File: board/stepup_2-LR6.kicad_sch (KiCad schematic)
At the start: 17 parts

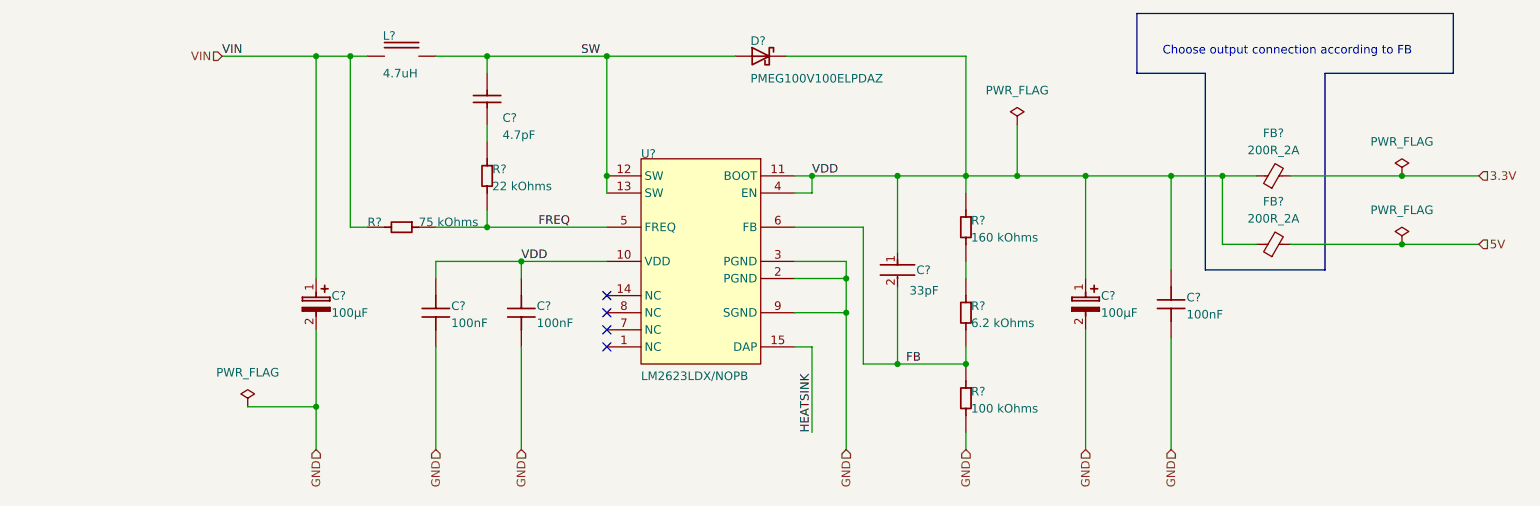
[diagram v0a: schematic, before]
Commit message: switched edge connectors to use the correct footprints and renamed local libraries to fit with the edgy naming convention
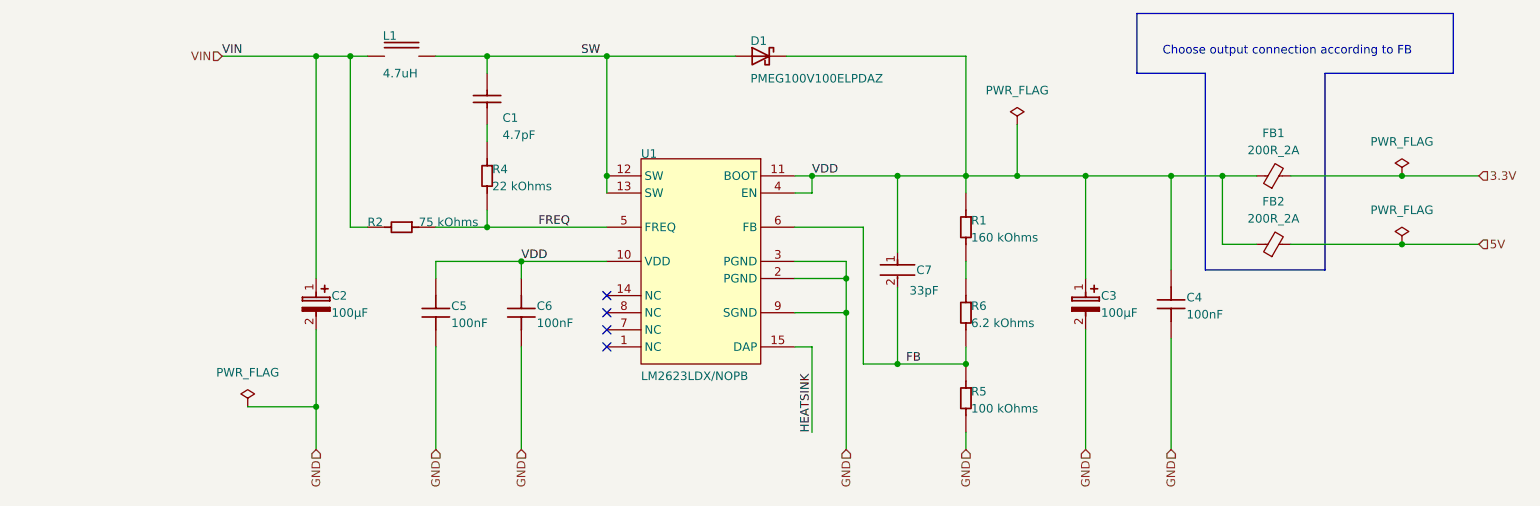
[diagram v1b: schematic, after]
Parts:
- C2, C3: renamed from C?; footprint stpup:CAPMP7344X43-T_V -> b132:CAPMP7344X43-T_V
- D1: renamed from D?; footprint stpup:PMEG100V100ELPDAZ -> b132:PMEG100V100ELPDAZ
- L1: renamed from L?; footprint stpup:WURTH 5040 -> b132:WURTH 5040
- U1: renamed from U?; footprint stpup:NHE0014A_V -> b132:NHE0014A_V
- gave numbers to parts that had none: 12
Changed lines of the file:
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@@
   (symbol (lib_id "step-up_2cell:1_Capacitor") (at 111.76 113.03 0) (unit 1)
     (in_bom yes) (on_board yes)
-    (property "Reference" "C?" (id 0) (at 114.046 112.776 0)
+    (property "Reference" "C5" (id 0) (at 114.046 112.776 0)
       (effects (font (size 1.27 1.27)) (justify left bottom))
     )
@@
   (symbol (lib_id "Device:FerriteBead_Small") (at 236.22 102.87 90) (unit 1)
     (in_bom yes) (on_board yes) (fields_autoplaced)
-    (property "Reference" "FB?" (id 0) (at 236.1819 96.52 90))
+    (property "Reference" "FB2" (id 0) (at 236.1819 96.52 90))
     (property "Value" "200R_2A" (id 1) (at 236.1819 99.06 90))
     (property "Footprint" "Inductor_SMD:L_0805_2012Metric" (id 2) (at 236.22 104.648 90)
@@
   (symbol (lib_id "step-up_2cell:3_T495X477K010ATE100") (at 208.28 107.95 0) (unit 1)
     (in_bom yes) (on_board yes)
-    (property "Reference" "C?" (id 0) (at 210.566 111.252 0)
+    (property "Reference" "C3" (id 0) (at 210.566 111.252 0)
       (effects (font (size 1.27 1.27)) (justify left bottom))
     )
@@
       (effects (font (size 1.27 1.27)) (justify left bottom) hide)
     )
-    (property "Footprint" "stpup:CAPMP7344X43-T_V" (id 2) (at 208.28 107.95 0)
+    (property "Footprint" "b132:CAPMP7344X43-T_V" (id 2) (at 208.28 107.95 0)
       (effects (font (size 1.27 1.27)) hide)
     )
@@
   (symbol (lib_id "power:PWR_FLAG") (at 255.27 92.71 0) (unit 1)
     (in_bom yes) (on_board yes) (fields_autoplaced)
-    (property "Reference" "#FLG?" (id 0) (at 255.27 90.805 0)
+    (property "Reference" "#FLG0103" (id 0) (at 255.27 90.805 0)
       (effects (font (size 1.27 1.27)) hide)
     )
@@
   (symbol (lib_id "step-up_2cell:0_Inductor") (at 106.68 74.93 0) (unit 1)
     (in_bom yes) (on_board yes)
-    (property "Reference" "L?" (id 0) (at 103.886 72.644 0)
+    (property "Reference" "L1" (id 0) (at 103.886 72.644 0)
       (effects (font (size 1.27 1.27)) (justify left bottom))
     )
@@
       (effects (font (size 1.27 1.27)) (justify left bottom))
     )
-    (property "Footprint" "stpup:WURTH 5040" (id 2) (at 106.68 74.93 0)
+    (property "Footprint" "b132:WURTH 5040" (id 2) (at 106.68 74.93 0)
       (effects (font (size 1.27 1.27)) hide)
     )
@@
   (symbol (lib_id "step-up_2cell:1_Resistor") (at 190.5 113.03 0) (unit 1)
     (in_bom yes) (on_board yes)
-    (property "Reference" "R?" (id 0) (at 191.262 112.776 0)
+    (property "Reference" "R6" (id 0) (at 191.262 112.776 0)
       (effects (font (size 1.27 1.27)) (justify left bottom))
     )
@@
   (symbol (lib_id "power:PWR_FLAG") (at 198.12 85.09 0) (unit 1)
     (in_bom yes) (on_board yes) (fields_autoplaced)
-    (property "Reference" "#FLG?" (id 0) (at 198.12 83.185 0)
+    (property "Reference" "#FLG0101" (id 0) (at 198.12 83.185 0)
       (effects (font (size 1.27 1.27)) hide)
     )
@@
   (symbol (lib_id "step-up_2cell:1_Capacitor") (at 220.98 111.76 0) (unit 1)
     (in_bom yes) (on_board yes)
-    (property "Reference" "C?" (id 0) (at 223.266 111.506 0)
+    (property "Reference" "C4" (id 0) (at 223.266 111.506 0)
       (effects (font (size 1.27 1.27)) (justify left bottom))
     )
@@
   (symbol (lib_id "Device:FerriteBead_Small") (at 236.22 92.71 90) (unit 1)
     (in_bom yes) (on_board yes) (fields_autoplaced)
-    (property "Reference" "FB?" (id 0) (at 236.1819 86.36 90))
+    (property "Reference" "FB1" (id 0) (at 236.1819 86.36 90))
     (property "Value" "200R_2A" (id 1) (at 236.1819 88.9 90))
     (property "Footprint" "Inductor_SMD:L_0805_2012Metric" (id 2) (at 236.22 94.488 90)
@@
   (symbol (lib_id "step-up_2cell:0_PM-DCDC-LM2623LD-15") (at 142.24 90.17 0) (unit 1)
     (in_bom yes) (on_board yes)
-    (property "Reference" "U?" (id 0) (at 142.24 90.17 0)
+    (property "Reference" "U1" (id 0) (at 142.24 90.17 0)
       (effects (font (size 1.27 1.27)) (justify left bottom))
     )
@@
       (effects (font (size 1.27 1.27)) (justify left bottom))
     )
-    (property "Footprint" "stpup:NHE0014A_V" (id 2) (at 142.24 90.17 0)
+    (property "Footprint" "b132:NHE0014A_V" (id 2) (at 142.24 90.17 0)
       (effects (font (size 1.27 1.27)) hide)
     )
@@
   (symbol (lib_id "step-up_2cell:3_T495X477K010ATE100") (at 93.98 107.95 0) (unit 1)
     (in_bom yes) (on_board yes)
-    (property "Reference" "C?" (id 0) (at 96.266 111.252 0)
+    (property "Reference" "C2" (id 0) (at 96.266 111.252 0)
       (effects (font (size 1.27 1.27)) (justify left bottom))
     )
@@
       (effects (font (size 1.27 1.27)) (justify left bottom) hide)
     )
-    (property "Footprint" "stpup:CAPMP7344X43-T_V" (id 2) (at 93.98 107.95 0)
+    (property "Footprint" "b132:CAPMP7344X43-T_V" (id 2) (at 93.98 107.95 0)
       (effects (font (size 1.27 1.27)) hide)
     )
@@
   (symbol (lib_id "step-up_2cell:1_Resistor") (at 190.5 125.73 0) (unit 1)
     (in_bom yes) (on_board yes)
-    (property "Reference" "R?" (id 0) (at 191.262 125.476 0)
+    (property "Reference" "R5" (id 0) (at 191.262 125.476 0)
       (effects (font (size 1.27 1.27)) (justify left bottom))
     )
@@
   (symbol (lib_id "step-up_2cell:0_b4654b650e69147ec39a6b967a45e02") (at 180.34 104.14 0) (unit 1)
     (in_bom yes) (on_board yes)
-    (property "Reference" "C?" (id 0) (at 183.134 107.442 0)
+    (property "Reference" "C7" (id 0) (at 183.134 107.442 0)
       (effects (font (size 1.27 1.27)) (justify left bottom))
     )
@@
   (symbol (lib_id "step-up_2cell:1_CAP-NP-2") (at 119.38 85.09 0) (unit 1)
     (in_bom yes) (on_board yes)
-    (property "Reference" "C?" (id 0) (at 121.666 84.836 0)
+    (property "Reference" "C1" (id 0) (at 121.666 84.836 0)
       (effects (font (size 1.27 1.27)) (justify left bottom))
     )
@@
   (symbol (lib_id "step-up_2cell:1_Capacitor") (at 124.46 113.03 0) (unit 1)
     (in_bom yes) (on_board yes)
-    (property "Reference" "C?" (id 0) (at 126.746 112.776 0)
+    (property "Reference" "C6" (id 0) (at 126.746 112.776 0)
       (effects (font (size 1.27 1.27)) (justify left bottom))
     )
@@
   (symbol (lib_id "step-up_2cell:0_Resistor") (at 106.68 100.33 0) (unit 1)
     (in_bom yes) (on_board yes)
-    (property "Reference" "R?" (id 0) (at 101.6 100.33 0)
+    (property "Reference" "R2" (id 0) (at 101.6 100.33 0)
       (effects (font (size 1.27 1.27)) (justify left bottom))
     )
@@
   (symbol (lib_id "power:PWR_FLAG") (at 83.82 127 0) (unit 1)
     (in_bom yes) (on_board yes) (fields_autoplaced)
-    (property "Reference" "#FLG?" (id 0) (at 83.82 125.095 0)
+    (property "Reference" "#FLG0102" (id 0) (at 83.82 125.095 0)
       (effects (font (size 1.27 1.27)) hide)
     )
@@
   (symbol (lib_id "power:PWR_FLAG") (at 255.27 102.87 0) (unit 1)
     (in_bom yes) (on_board yes) (fields_autoplaced)
-    (property "Reference" "#FLG?" (id 0) (at 255.27 100.965 0)
+    (property "Reference" "#FLG0104" (id 0) (at 255.27 100.965 0)
       (effects (font (size 1.27 1.27)) hide)
     )
@@
   (symbol (lib_id "step-up_2cell:1_Resistor") (at 190.5 100.33 0) (unit 1)
     (in_bom yes) (on_board yes)
-    (property "Reference" "R?" (id 0) (at 191.262 100.076 0)
+    (property "Reference" "R1" (id 0) (at 191.262 100.076 0)
       (effects (font (size 1.27 1.27)) (justify left bottom))
     )
@@
   (symbol (lib_id "step-up_2cell:1_Resistor") (at 119.38 92.71 0) (unit 1)
     (in_bom yes) (on_board yes)
-    (property "Reference" "R?" (id 0) (at 120.142 92.456 0)
+    (property "Reference" "R4" (id 0) (at 120.142 92.456 0)
       (effects (font (size 1.27 1.27)) (justify left bottom))
     )
@@
   (symbol (lib_id "step-up_2cell:0_mirrored_PMEG100V100ELPD") (at 161.29 74.93 0) (unit 1)
     (in_bom yes) (on_board yes)
-    (property "Reference" "D?" (id 0) (at 158.496 73.406 0)
+    (property "Reference" "D1" (id 0) (at 158.496 73.406 0)
       (effects (font (size 1.27 1.27)) (justify left bottom))
     )
@@
       (effects (font (size 1.27 1.27)) (justify left bottom))
     )
-    (property "Footprint" "stpup:PMEG100V100ELPDAZ" (id 2) (at 161.29 74.93 0)
-      (effects (font (size 1.27 1.27)) hide)
-    )
+    (property "Footprint" "b132:PMEG100V100ELPDAZ" (id 2) (at 161.29 74.93 0)
+      (effects (font (size 1.27 1.27)) hide)
+    )

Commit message: changed constraints to work as a 2 layer board, changed symbols to kicad native
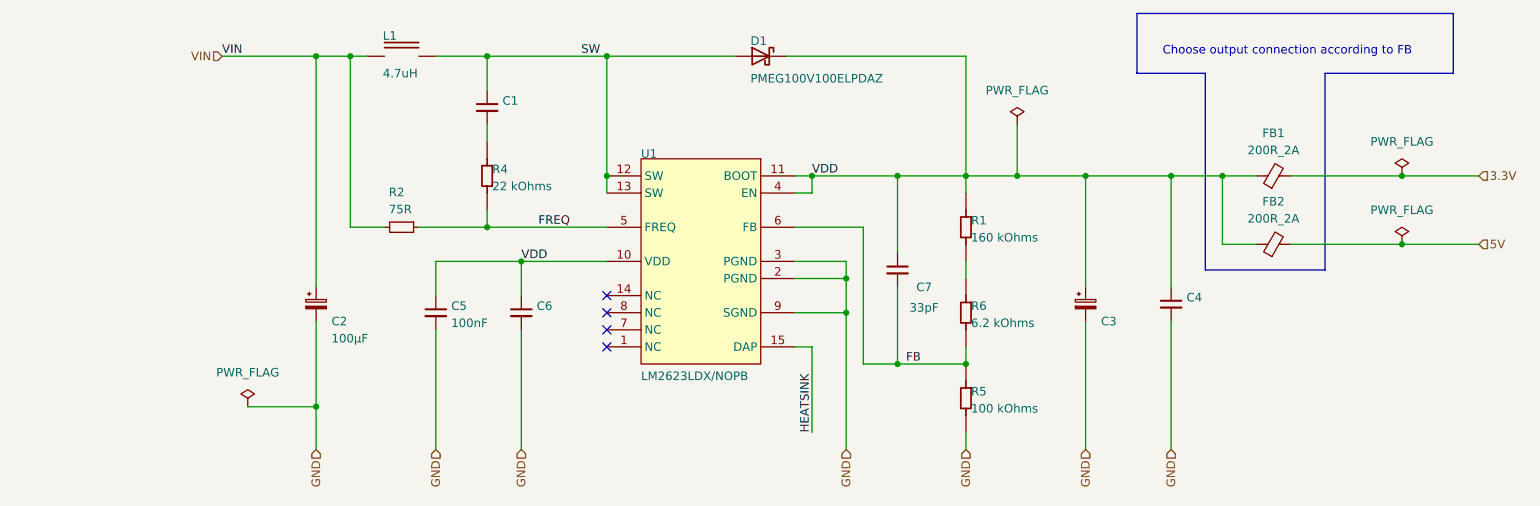
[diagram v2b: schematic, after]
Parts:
- C1: symbol step-up_2cell:1_CAP-NP-2 -> Device:C_Small; ALTIUM_VALUE 4.7pF -> (none); CAPACITOR TYPE Ceramic -> (none); KICADVALUE 4.7pF -> (none); MAX OPERATING TEMPERATURE 125°C -> (none); MIN OPERATING TEMPERATURE -55°C -> (none); PACKAGE / CASE 0402 (1005 Metric) -> (none); ROHS COMPLIANT Yes -> (none)
- C2: symbol step-up_2cell:3_T495X477K010ATE100 -> Device:C_Polarized_Small
- C3: symbol step-up_2cell:3_T495X477K010ATE100 -> Device:C_Polarized_Small; ALTIUM_VALUE 100µF -> (none); CAPACITOR TYPE Tantalum -> (none); CASE/PACKAGE Rectangular -> (none); CATEGORY Tantalum Capacitors -> (none); COMPONENTLINK10DESCRIPTION https://datasheet.ciiva.com/7720/1680477-7720758.pdf?src-su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 -> (none); COMPONENTLINK10URL https://datasheet.ciiva.com/7720/1680477-7720758.pdf?src-su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 -> (none); COMPONENTLINK11DESCRIPTION https://datasheet.ciiva.com/11231/tps-11231830.pdf?src-supp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 -> (none); COMPONENTLINK11URL https://datasheet.ciiva.com/11231/tps-11231830.pdf?src-supp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 -> (none); COMPONENTLINK12DESCRIPTION https://datasheet.ciiva.com/14602/70001047-14602166.pdf?src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 -> (none); COMPONENTLINK12URL https://datasheet.ciiva.com/14602/70001047-14602166.pdf?src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 -> (none); COMPONENTLINK13DESCRIPTION https://datasheet.ciiva.com/7720/1680477-7720759.pdf?src-su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 -> (none); COMPONENTLINK13URL https://datasheet.ciiva.com/7720/1680477-7720759.pdf?src-su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 -> (none); COMPONENTLINK14DESCRIPTION https://datasheet.ciiva.com/7720/1441576-7720760.pdf?src-su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 -> (none); COMPONENTLINK14URL https://datasheet.ciiva.com/7720/1441576-7720760.pdf?src-su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 -> (none); COMPONENTLINK15DESCRIPTION https://datasheet.ciiva.com/12911/tps-23028-12911514.pdf?sr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 -> (none); COMPONENTLINK15URL https://datasheet.ciiva.com/12911/tps-23028-12911514.pdf?sr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 -> (none); COMPONENTLINK16DESCRIPTION https://datasheet.ciiva.com/15163/getdatasheetpartid-75405-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 -> (none); COMPONENTLINK16URL https://datasheet.ciiva.com/15163/getdatasheetpartid-75405-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 -> (none); COMPONENTLINK17DESCRIPTION https://datasheet.ciiva.com/18710/tps-eng-18710830.pdf?src-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 -> (none); COMPONENTLINK17URL https://datasheet.ciiva.com/18710/tps-eng-18710830.pdf?src-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 -> (none); COMPONENTLINK1DESCRIPTION https://datasheet.ciiva.com:443/pdfs/VipMasterIC/IC/AVXC/AV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 -> (none); COMPONENTLINK1URL https://datasheet.ciiva.com:443/pdfs/VipMasterIC/IC/AVXC/AV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 -> (none); COMPONENTLINK2DESCRIPTION https://datasheet.ciiva.com/11793/0900766b80962b61-11793069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 -> (none); COMPONENTLINK2URL https://datasheet.ciiva.com/11793/0900766b80962b61-11793069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 -> (none); COMPONENTLINK3DESCRIPTION https://datasheet.ciiva.com/26341/806585-da-01-en-smd-tanta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 -> (none); COMPONENTLINK3URL https://datasheet.ciiva.com/26341/806585-da-01-en-smd-tanta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 -> (none); COMPONENTLINK4DESCRIPTION https://datasheet.ciiva.com/265/tps-265666.pdf?src-supplier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 -> (none); COMPONENTLINK4URL https://datasheet.ciiva.com/265/tps-265666.pdf?src-supplier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 -> (none); COMPONENTLINK5DESCRIPTION https://datasheet.ciiva.com/265/tps-265667.pdf?src-supplier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 -> (none); COMPONENTLINK5URL https://datasheet.ciiva.com/265/tps-265667.pdf?src-supplier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 -> (none); COMPONENTLINK6DESCRIPTION https://datasheet.ciiva.com/265/tps-265668.pdf?src-supplier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 -> (none); COMPONENTLINK6URL https://datasheet.ciiva.com/265/tps-265668.pdf?src-supplier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 -> (none); COMPONENTLINK7DESCRIPTION https://datasheet.ciiva.com/7720/1680477-7720757.pdf?src-su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 -> (none); COMPONENTLINK7URL https://datasheet.ciiva.com/7720/1680477-7720757.pdf?src-su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 -> (none); COMPONENTLINK8DESCRIPTION https://datasheet.ciiva.com/16392/tps-16392933.pdf?src-supp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 -> (none); COMPONENTLINK8URL https://datasheet.ciiva.com/16392/tps-16392933.pdf?src-supp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 -> (none); COMPONENTLINK9DESCRIPTION https://datasheet.ciiva.com/7092/1808765-7092710.pdf?src-su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 -> (none); COMPONENTLINK9URL https://datasheet.ciiva.com/7092/1808765-7092710.pdf?src-su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 -> (none); DESIGN ITEM ID TPSE107K016R0100 -> (none); DIELECTRIC MATERIAL Tantalum -> (none); ESR (EQUIVALENT SERIES RESISTANCE) 0.1 -> (none); HEIGHT 4.1mm -> (none); JESD-609 CODE e3 -> (none); KICADVALUE 100µF -> (none); LEAKAGE CURRENT 16uA -> (none); LENGTH 7.3mm -> (none); MANUFACTURER Kyocera AVX -> (none); MANUFACTURER PART NUMBER TPSE107K016R0100 -> (none); MAX OPERATING TEMPERATURE 125°C -> (none); MIN OPERATING TEMPERATURE -55°C -> (none); MOUNT Surface Mount -> (none); NEGATIVE TOLERANCE 10% -> (none); PACKAGE STYLE SMTMeter -> (none); PACKAGING Tape and Reel -> (none); PINS 2 -> (none); POLARITY Polarized -> (none); POSITIVE TOLERANCE 10% -> (none); PRICING 1 1=2,31420, 10=1,89070, 25=1,75590 (USD) -> (none); RATED DC VOLTAGE (URDC) 16V -> (none); REACH SVHC Yes -> (none); ROHS Yes -> (none); ROHS COMPLIANT Yes -> (none); SIZE CODE 2917 -> (none); SOURCE sweep4fun_on_kria-k26.SchLib -> (none); STOCK 1 31 -> (none); TAN DELTA 0.06 -> (none); TERMINAL FINISH Nickel -> (none); TERMINATION J BEND -> (none); WIDTH 4.3mm -> (none)
- C4, C6: symbol step-up_2cell:1_Capacitor -> Device:C_Small; ALTIUM_VALUE 100nF -> (none); APPLICATIONS Automotive -> (none); CAPACITANCE 0.1 µF -> (none); COMPONENTLINK1DESCRIPTION Datasheet -> (none); COMPONENTLINK1URL http://www.yageo.com/documents/recent/UPY-AC_NP0X7R_16V-to-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 -> (none); COMPONENTLINK2DESCRIPTION DigiKey Link -> (none); COMPONENTLINK2URL https://www.digikey.com/en/products/detail/yageo/AC0402KRX7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 -> (none); DEVICE PACKAGE 0402 (1005 Metric) -> (none); KICADVALUE 0.1 µF -> (none); LASTUPDATED 01/09/2022 12:30:48 -> (none); LIFECYCLE STATUS Active -> (none); MANUFACTURER Yageo -> (none); MINIMUM ORDER 1 -> (none); MOUNTING TYPE Surface Mount, MLCC -> (none); OPERATING TEMPERATURE -55°C ~ 125°C -> (none); PACKAGE / CASE 0402 (1005 Metric) -> (none); PACKAGING TapeAndReel -> (none); PART NUMBER AC0402KRX7R7BB104 -> (none); PART STATUS Active -> (none); PARTID 2724 -> (none); PRICE 0.01 -> (none); RATINGS AEC-Q200 -> (none); SERIES AC -> (none); SIZE / DIMENSION 0.039" L x 0.020" W (1.00mm x 0.50mm) -> (none); SUPPLIER 1 DigiKey -> (none); SUPPLIER PART NUMBER 1 311-3026-1-ND -> (none); TEMPERATURE COEFFICIENT X7R -> (none); THICKNESS (MAX) 0.022" (0.55mm) -> (none); TOLERANCE ±10% -> (none); VOLTAGE - RATED 16V -> (none)
- C5: symbol step-up_2cell:1_Capacitor -> Device:C_Small
- C7: symbol step-up_2cell:0_b4654b650e69147ec39a6b967a45e02 -> Device:C_Small
- R2: value 75 kOhms -> 75R; symbol step-up_2cell:0_Resistor -> Device:R_Small; ALTIUM_VALUE 75 kOhms -> (none); COMPONENTLINK1DESCRIPTION Datasheet -> (none); COMPONENTLINK1URL http://www.vishay.com/docs/20035/dcrcwe3.pdf -> (none); COMPONENTLINK2DESCRIPTION DigiKey Link -> (none); COMPONENTLINK2URL https://www.digikey.com/en/products/detail/vishay-dale/CRCW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 -> (none); COMPOSITION Thick Film -> (none); DEVICE PACKAGE 0402 (1005 Metric) -> (none); FEATURES Automotive AEC-Q200 -> (none); HEIGHT - SEATED (MAX) 0.016" (0.40mm) -> (none); LASTUPDATED 02/01/2023 20:20:52 -> (none); LIFECYCLE STATUS Active -> (none); MANUFACTURER Vishay Dale -> (none); MINIMUM ORDER 1 -> (none); NUMBER OF TERMINATIONS 2 -> (none); OPERATING TEMPERATURE -55°C ~ 155°C -> (none); PACKAGE / CASE 0402 (1005 Metric) -> (none); PACKAGING CutTape -> (none); PART NUMBER CRCW040275K0FKED -> (none); PART STATUS Active -> (none); PARTID 16215 -> (none); POWER (WATTS) 0.063W, 1/16W -> (none); PRICE 0.01 -> (none); RATINGS AEC-Q200 -> (none); RESISTANCE 75 kOhms -> (none); SERIES CRCW -> (none); SIZE / DIMENSION 0.039" L x 0.020" W (1.00mm x 0.50mm) -> (none); SUPPLIER 1 DigiKey -> (none); SUPPLIER DEVICE PACKAGE 0402 -> (none); SUPPLIER PART NUMBER 1 541-75.0KLCT-ND -> (none); TEMPERATURE COEFFICIENT ±100ppm/°C -> (none); TOLERANCE ±1% -> (none)
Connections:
- net FREQ: now also R2.1; no longer R2.2
- net GND: now also C4.2, C5.2, C6.2; no longer C4.1, C5.1, C6.1
- net SW: now also C1.1; no longer C1.2
- net VDD: now also C4.1, C5.1, C6.1; no longer C4.2, C5.2, C6.2
- net VIN: now also R2.2; no longer R2.1
- net at R4.2: now also C1.2; no longer C1.1

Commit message: switched to ceramic caps
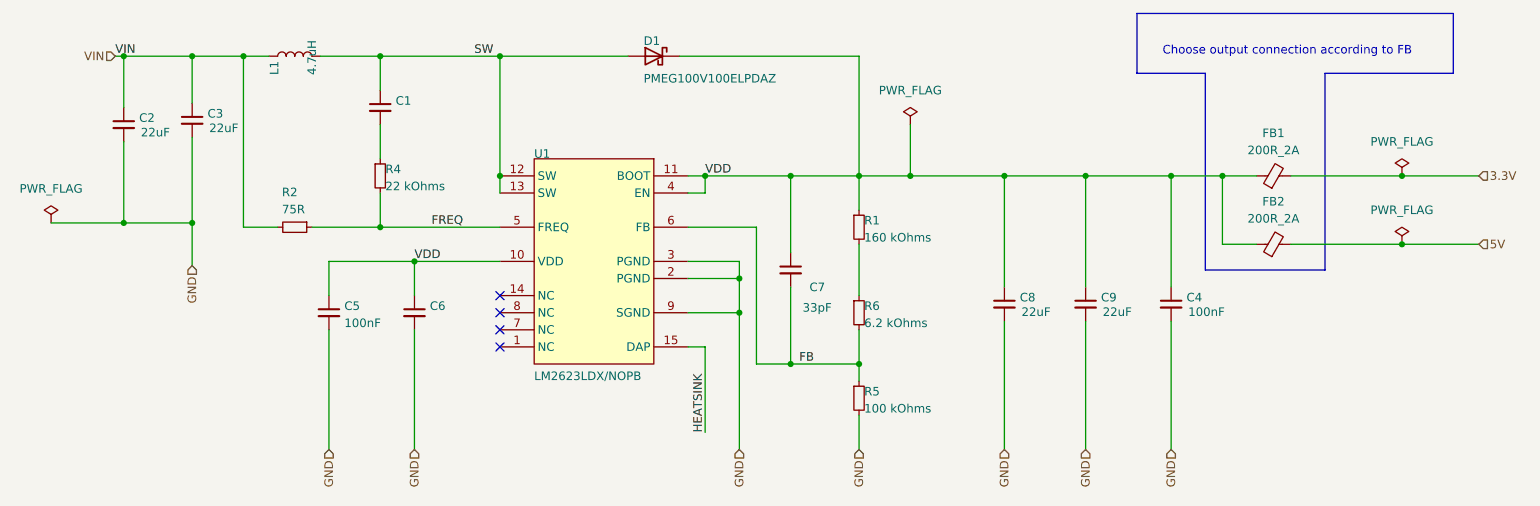
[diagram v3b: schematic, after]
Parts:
- removed C2, C3: TPSE107K016R0100, b132:CAPMP7344X43-T_V, symbol Device:C_Polarized_Small
- added C2, C3, C8, C9: 22uF, Capacitor_SMD:C_0805_2012Metric, symbol Device:C_Small
- L1: symbol step-up_2cell:0_Inductor -> Device:L
- R1, R4, R5, R6: symbol step-up_2cell:1_Resistor -> Device:R_Small
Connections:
- net FB: now also R5.1, R6.2; no longer R5.2, R6.1
- net FREQ: now also R4.2; no longer R4.1
- net GND: now also R5.2, C2.2, C3.2, C8.2, C9.2; no longer R5.1
- net VDD: now also R1.1, C8.1, C9.1; no longer R1.2
- net VIN: now also C2.1, C3.1
- net at C1.2: now also R4.1; no longer R4.2
- new net: R1.2, R6.1
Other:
- moved on the sheet: C1, C5, C6, C7, D1, R2, U1
